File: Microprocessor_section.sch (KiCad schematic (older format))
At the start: 14 parts, among them J15 Conn_01x06_Male, SW1 K2-1102SP-C4SC-04, U5 ESP32-WROOM-32D

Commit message: Export fabrication files
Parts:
- J15: LCSC (none) -> C124380
- JP3, JP4: LCSC (none) -> C160332
- U5: LCSC (none) -> C473012
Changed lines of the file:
@@
 F 2 "Connector_PinHeader_2.54mm:PinHeader_1x06_P2.54mm_Vertical" H 2000 2200 50  0001 C CNN
 F 3 "~" H 2000 2200 50  0001 C CNN
+F 4 "C124380" H 2000 2200 50  0001 C CNN "LCSC"
 	1    2000 2200
 	1    0    0    -1
@@
 F 2 "RF_Module:ESP32-WROOM-32" H 6500 2500 50  0001 C CNN
 F 3 "https://www.espressif.com/sites/default/files/documentation/esp32-wroom-32d_esp32-wroom-32u_datasheet_en.pdf" H 6200 4050 50  0001 C CNN
+F 4 "C473012" H 6500 4000 50  0001 C CNN "LCSC"
 	1    6500 4000
 	1    0    0    -1
@@
 F 2 "Connector_PinHeader_2.54mm:PinHeader_1x02_P2.54mm_Vertical" H 2000 4100 50  0001 C CNN
 F 3 "~" H 2000 4100 50  0001 C CNN
+F 4 "C160332" H 2000 4100 50  0001 C CNN "LCSC"
 	1    2000 4100
 	1    0    0    1
@@
 F 2 "Connector_PinHeader_2.54mm:PinHeader_1x02_P2.54mm_Vertical" H 3800 4000 50  0001 C CNN
 F 3 "~" H 3800 4000 50  0001 C CNN
+F 4 "C160332" H 3800 4000 50  0001 C CNN "LCSC"
 	1    3800 4000
 	1    0    0    -1

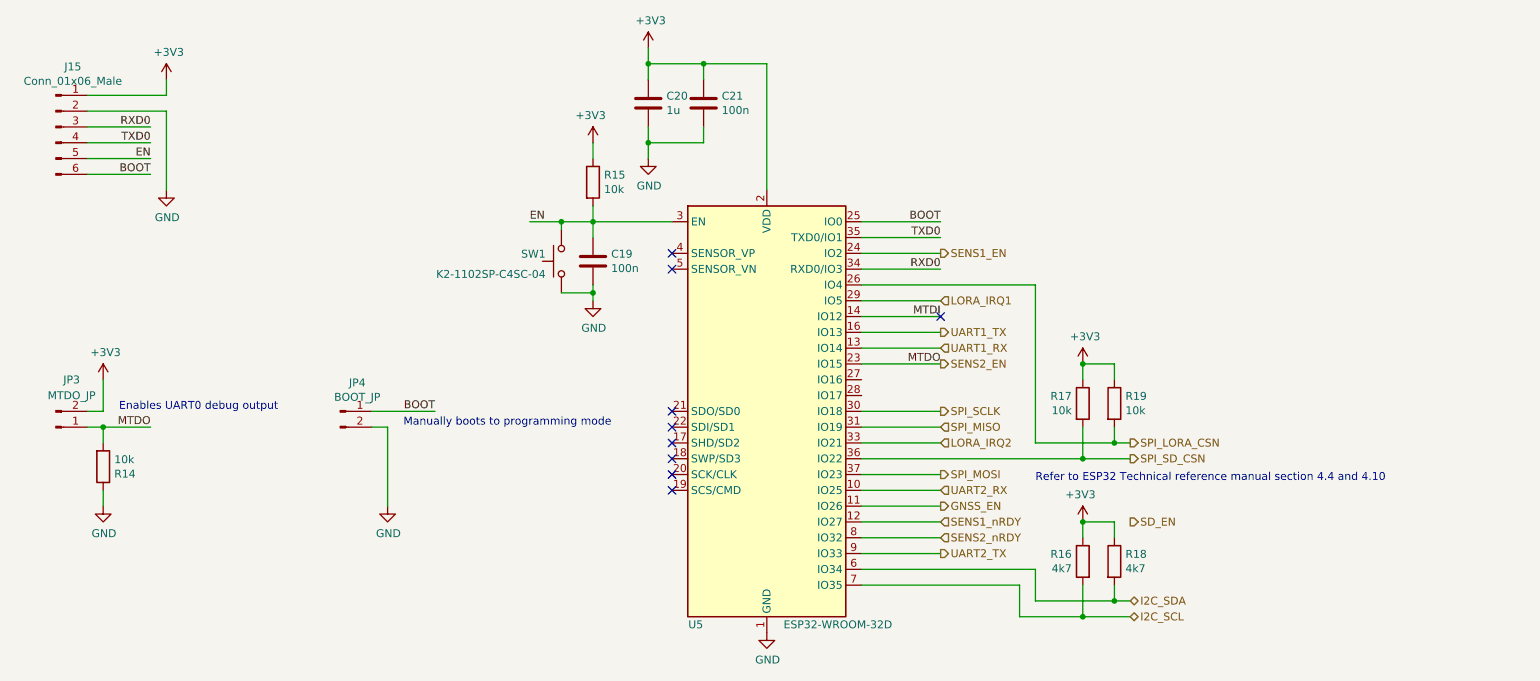
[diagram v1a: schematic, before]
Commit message: Start changing design for long term chambers
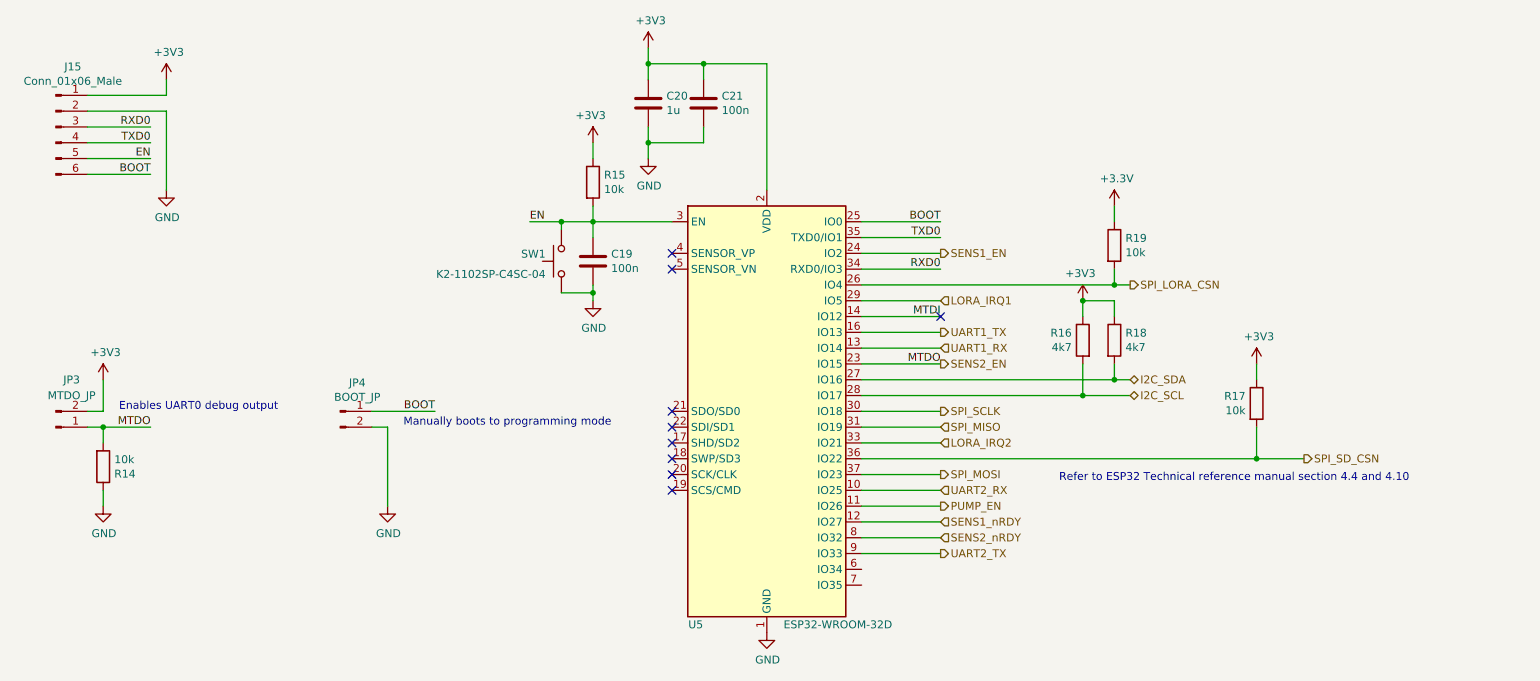
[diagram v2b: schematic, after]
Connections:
- net I2C_SCL: now also U5.28 (IO17); no longer U5.7 (IO35)
- net I2C_SDA: now also U5.27 (IO16); no longer U5.6 (IO34)
- net GNSS_EN renamed PUMP_EN
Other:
- moved on the sheet: R16, R17, R18, R19
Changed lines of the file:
@@
 $Descr A4 11693 8268
 encoding utf-8
-Sheet 9 9
+Sheet 8 9
 Title ""
 Date ""
@@
 $EndComp
 Wire Wire Line
-	8500 5100 8500 5300
-Wire Wire Line
-	8500 5300 8800 5300
-Connection ~ 8500 4700
-Wire Wire Line
-	8700 4200 8800 4200
-Connection ~ 8700 4200
-Wire Wire Line
-	8700 4100 8700 4200
-Wire Wire Line
-	8500 4300 8800 4300
-Connection ~ 8500 4300
-Wire Wire Line
-	8500 4100 8500 4300
-Wire Wire Line
-	8700 5200 8800 5200
-Wire Wire Line
-	8500 4700 8700 4700
-Wire Wire Line
-	8500 3700 8700 3700
-Wire Wire Line
-	8700 3700 8700 3800
+	8700 3200 8800 3200
+Connection ~ 8700 3200
+Wire Wire Line
+	8700 3100 8700 3200
 $Comp
 L power:GND #PWR064
@@
 	7100 4800 7600 4800
 Wire Wire Line
-	7100 4600 7600 4600
-Wire Wire Line
 	7100 4700 7600 4700
 Wire Wire Line
@@
 Text HLabel 7600 4000 2    50   Output ~ 0
 SPI_SCLK
-Text HLabel 8800 4700 2    50   Output ~ 0
-SD_EN
 Text HLabel 7600 4200 2    50   Input ~ 0
 LORA_IRQ2
 Text HLabel 7600 3300 2    50   Input ~ 0
 LORA_IRQ1
-Text HLabel 7600 4600 2    50   Output ~ 0
-GNSS_EN
 Text HLabel 7600 4800 2    50   Input ~ 0
 SENS2_nRDY
@@
 	6100 1800 5750 1800
 Connection ~ 6100 1800
-Connection ~ 8500 3700
-Wire Wire Line
-	8500 3800 8500 3700
-$Comp
-L power:+3V3 #PWR066
-U 1 1 60A5A46E
-P 8500 3700
-F 0 "#PWR066" H 8500 3550 50  0001 C CNN
-F 1 "+3V3" H 8515 3873 50  0000 C CNN
-F 2 "" H 8500 3700 50  0001 C CNN
-F 3 "" H 8500 3700 50  0001 C CNN
-	1    8500 3700
-	1    0    0    -1
-$EndComp
 $Comp
 L Device:R R19
 U 1 1 60A5A468
-P 8700 3950
-F 0 "R19" H 8770 3996 50  0000 L CNN
-F 1 "10k" H 8770 3905 50  0000 L CNN
-F 2 "Resistor_SMD:R_0603_1608Metric" V 8630 3950 50  0001 C CNN
-F 3 "~" H 8700 3950 50  0001 C CNN
-F 4 "C25804" H 8700 3950 50  0001 C CNN "LCSC"
-	1    8700 3950
-	1    0    0    -1
-$EndComp
-$Comp
-L Device:R R17
-U 1 1 60A5A462
-P 8500 3950
-F 0 "R17" H 8430 3996 50  0000 R CNN
-F 1 "10k" H 8430 3905 50  0000 R CNN
-F 2 "Resistor_SMD:R_0603_1608Metric" V 8430 3950 50  0001 C CNN
-F 3 "~" H 8500 3950 50  0001 C CNN
-F 4 "C25804" H 8500 3950 50  0001 C CNN "LCSC"
-	1    8500 3950
-	1    0    0    -1
-$EndComp
-Wire Wire Line
-	8500 4800 8500 4700
-Wire Wire Line
-	8700 4800 8700 4700
-Wire Wire Line
-	8700 5200 8700 5100
-$Comp
-L power:+3V3 #PWR065
-U 1 1 60A5400B
-P 8500 4700
-F 0 "#PWR065" H 8500 4550 50  0001 C CNN
-F 1 "+3V3" H 8515 4873 50  0000 C CNN
-F 2 "" H 8500 4700 50  0001 C CNN
-F 3 "" H 8500 4700 50  0001 C CNN
-	1    8500 4700
-	-1   0    0    -1
-$EndComp
-$Comp
-L Device:R R16
-U 1 1 60A50D69
-P 8500 4950
-F 0 "R16" H 8570 4996 50  0000 L CNN
-F 1 "4k7" H 8570 4905 50  0000 L CNN
-F 2 "Resistor_SMD:R_0603_1608Metric" V 8430 4950 50  0001 C CNN
-F 3 "~" H 8500 4950 50  0001 C CNN
-F 4 "C23162" H 8500 4950 50  0001 C CNN "LCSC"
-	1    8500 4950
-	-1   0    0    -1
-$EndComp
-$Comp
-L Device:R R18
-U 1 1 60A501AF
-P 8700 4950
-F 0 "R18" H 8770 4996 50  0000 L CNN
-F 1 "4k7" H 8770 4905 50  0000 L CNN
-F 2 "Resistor_SMD:R_0603_1608Metric" V 8630 4950 50  0001 C CNN
-F 3 "~" H 8700 4950 50  0001 C CNN
-F 4 "C23162" H 8700 4950 50  0001 C CNN "LCSC"
-	1    8700 4950
+P 8700 2950
+F 0 "R19" H 8770 2996 50  0000 L CNN
+F 1 "10k" H 8770 2905 50  0000 L CNN
+F 2 "Resistor_SMD:R_0603_1608Metric" V 8630 2950 50  0001 C CNN
+F 3 "~" H 8700 2950 50  0001 C CNN
+F 4 "C25804" H 8700 2950 50  0001 C CNN "LCSC"
+	1    8700 2950
 	1    0    0    -1
 $EndComp
@@
 Wire Wire Line
 	7600 3600 7100 3600
-Text HLabel 8800 4300 2    50   Output ~ 0
-SPI_SD_CSN
-Text HLabel 8800 4200 2    50   Output ~ 0
+Text HLabel 8800 3200 2    50   Output ~ 0
 SPI_LORA_CSN
-Text HLabel 8800 5200 2    50   BiDi ~ 0
-I2C_SDA
-Text HLabel 8800 5300 2    50   BiDi ~ 0
-I2C_SCL
 Text HLabel 7600 3600 2    50   Input ~ 0
 UART1_RX
@@
 Text HLabel 7600 4900 2    50   Output ~ 0
 UART2_TX
-Text Notes 8200 4450 0    50   ~ 0
-Refer to ESP32 Technical reference manual section 4.4 and 4.10\n
 NoConn ~ 7600 3400
 Wire Wire Line
@@
 	0    -1   -1   0
 $EndComp
-Connection ~ 8700 5200
-Connection ~ 8500 5300
-Wire Wire Line
-	7100 4300 8500 4300
-Wire Wire Line
-	7100 3200 8200 3200
-Wire Wire Line
-	8200 3200 8200 4200
-Wire Wire Line
-	8200 4200 8700 4200
-Wire Wire Line
-	8200 5200 8700 5200
-Wire Wire Line
-	8100 5300 8500 5300
-Wire Wire Line
-	7100 5000 8200 5000
-Wire Wire Line
-	8200 5000 8200 5200
-Wire Wire Line
-	8100 5300 8100 5100
-Wire Wire Line
-	8100 5100 7100 5100
+Wire Wire Line
+	7100 3200 8700 3200
+Text Notes 8350 4450 0    50   ~ 0
+Refer to ESP32 Technical reference manual section 4.4 and 4.10\n
+Text HLabel 9900 4300 2    50   Output ~ 0
+SPI_SD_CSN
+$Comp
+L Device:R R17
+U 1 1 60A5A462
+P 9600 3950
+F 0 "R17" H 9530 3996 50  0000 R CNN
+F 1 "10k" H 9530 3905 50  0000 R CNN
+F 2 "Resistor_SMD:R_0603_1608Metric" V 9530 3950 50  0001 C CNN
+F 3 "~" H 9600 3950 50  0001 C CNN
+F 4 "C25804" H 9600 3950 50  0001 C CNN "LCSC"
+	1    9600 3950
+	1    0    0    -1
+$EndComp
+$Comp
+L power:+3V3 #PWR066
+U 1 1 60A5A46E
+P 9600 3700
+F 0 "#PWR066" H 9600 3550 50  0001 C CNN
+F 1 "+3V3" H 9615 3873 50  0000 C CNN
+F 2 "" H 9600 3700 50  0001 C CNN
+F 3 "" H 9600 3700 50  0001 C CNN
+	1    9600 3700
+	1    0    0    -1
+$EndComp
+Wire Wire Line
+	9600 3800 9600 3700
+Wire Wire Line
+	9600 4100 9600 4300
+Connection ~ 9600 4300
+Wire Wire Line
+	9600 4300 9900 4300
+Connection ~ 8500 3900
+Connection ~ 8700 3800
+Text HLabel 8800 3900 2    50   BiDi ~ 0
+I2C_SCL
+Text HLabel 8800 3800 2    50   BiDi ~ 0
+I2C_SDA
+$Comp
+L Device:R R18
+U 1 1 60A501AF
+P 8700 3550
+F 0 "R18" H 8770 3596 50  0000 L CNN
+F 1 "4k7" H 8770 3505 50  0000 L CNN
+F 2 "Resistor_SMD:R_0603_1608Metric" V 8630 3550 50  0001 C CNN
+F 3 "~" H 8700 3550 50  0001 C CNN
+F 4 "C23162" H 8700 3550 50  0001 C CNN "LCSC"
+	1    8700 3550
+	1    0    0    -1
+$EndComp
+$Comp
+L Device:R R16
+U 1 1 60A50D69
+P 8500 3550
+F 0 "R16" H 8570 3596 50  0000 L CNN
+F 1 "4k7" H 8570 3505 50  0000 L CNN
+F 2 "Resistor_SMD:R_0603_1608Metric" V 8430 3550 50  0001 C CNN
+F 3 "~" H 8500 3550 50  0001 C CNN
+F 4 "C23162" H 8500 3550 50  0001 C CNN "LCSC"
+	1    8500 3550
+	-1   0    0    -1
+$EndComp
+$Comp
+L power:+3V3 #PWR065
+U 1 1 60A5400B
+P 8500 3300
+F 0 "#PWR065" H 8500 3150 50  0001 C CNN
+F 1 "+3V3" H 8515 3473 50  0000 C CNN
+F 2 "" H 8500 3300 50  0001 C CNN
+F 3 "" H 8500 3300 50  0001 C CNN
+	1    8500 3300
+	-1   0    0    -1
+$EndComp
+Wire Wire Line
+	8700 3800 8700 3700
+Wire Wire Line
+	8700 3400 8700 3300
+Wire Wire Line
+	8500 3400 8500 3300
+Wire Wire Line
+	8500 3300 8700 3300
+Wire Wire Line
+	8700 3800 8800 3800
+Connection ~ 8500 3300
+Wire Wire Line
+	8500 3900 8800 3900
+Wire Wire Line
+	8500 3700 8500 3900
+Wire Wire Line
+	7100 3900 8500 3900
+Wire Wire Line
+	7100 3800 8700 3800
+Wire Wire Line
+	7100 4300 9600 4300
+Text HLabel 7600 4600 2    50   Output ~ 0
+PUMP_EN
+Wire Wire Line
+	7100 4600 7600 4600
+$Comp
+L power:+3.3V #PWR?
+U 1 1 60C14EF9
+P 8700 2700
+F 0 "#PWR?" H 8700 2550 50  0001 C CNN
+F 1 "+3.3V" H 8715 2873 50  0000 C CNN
+F 2 "" H 8700 2700 50  0001 C CNN
+F 3 "" H 8700 2700 50  0001 C CNN
+	1    8700 2700
+	1    0    0    -1
+$EndComp
+Wire Wire Line
+	8700 2800 8700 2700
 $EndSCHEMATC

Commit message: Finalize schematic
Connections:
- net LORA_IRQ2: now also U5.6 (IO34); no longer U5.33 (IO21)
- new net TEMPSENSOR: U5.33 (IO21)
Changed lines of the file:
@@
 $EndComp
 Wire Wire Line
-	7100 4200 7600 4200
+	7100 5000 7600 5000
 Wire Wire Line
 	7100 3300 7600 3300
@@
 Text HLabel 7600 4000 2    50   Output ~ 0
 SPI_SCLK
-Text HLabel 7600 4200 2    50   Input ~ 0
+Text HLabel 7600 5000 2    50   Input ~ 0
 LORA_IRQ2
 Text HLabel 7600 3300 2    50   Input ~ 0
@@
 Wire Wire Line
 	8700 2800 8700 2700
+Text HLabel 7600 4200 2    50   Input ~ 0
+TEMPSENSOR
+Wire Wire Line
+	7100 4200 7600 4200
 $EndSCHEMATC

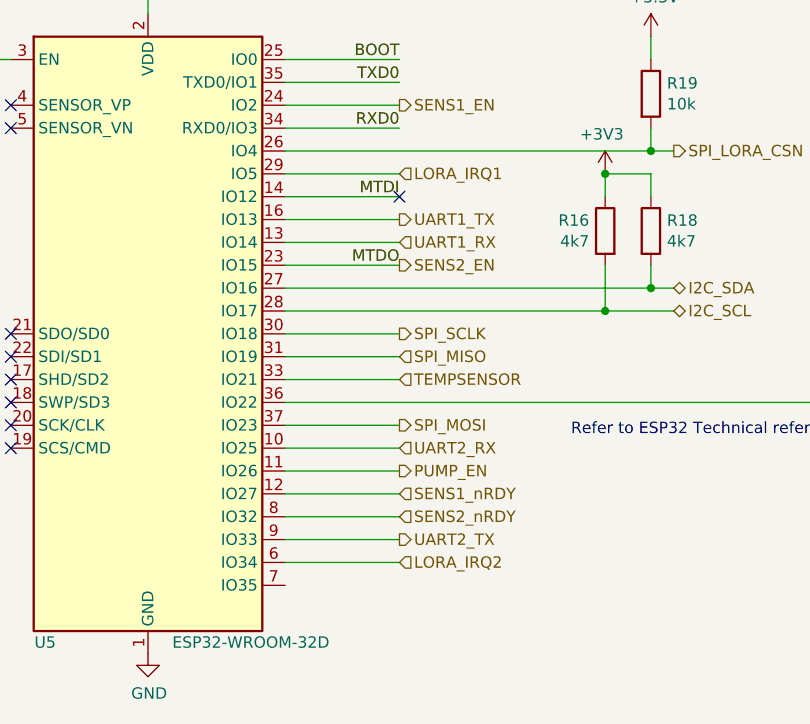
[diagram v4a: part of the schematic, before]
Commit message: Finish routing of Rev 1
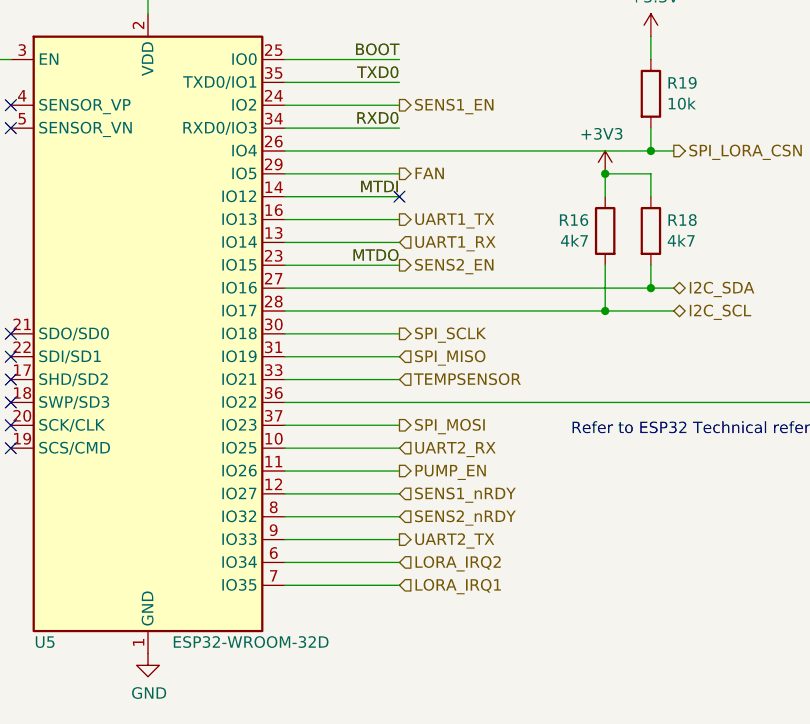
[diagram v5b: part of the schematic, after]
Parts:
- SW1: LCSC https://lcsc.com/product-detail/Tactile-Switches_Korean-Hro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 -> C127509
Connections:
- net LORA_IRQ1: now also U5.7 (IO35); no longer U5.29 (IO5)
- new net FAN: U5.29 (IO5)
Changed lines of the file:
@@
 $Descr A4 11693 8268
 encoding utf-8
-Sheet 8 9
+Sheet 8 10
 Title ""
 Date ""
@@
 	7100 5000 7600 5000
 Wire Wire Line
-	7100 3300 7600 3300
+	7100 5100 7600 5100
 Wire Wire Line
 	7100 4100 7600 4100
@@
 Text HLabel 7600 5000 2    50   Input ~ 0
 LORA_IRQ2
-Text HLabel 7600 3300 2    50   Input ~ 0
+Text HLabel 7600 5100 2    50   Input ~ 0
 LORA_IRQ1
 Text HLabel 7600 4800 2    50   Input ~ 0
@@
 F 2 "co2_sensor_node:K2-1102SP-xxxC" H 5200 3250 50  0001 C CNN
 F 3 "https://datasheet.lcsc.com/szlcsc/1811082113_Korean-Hroparts-Elec-K2-1102SP-C4SC-04_C127509.pdf" H 5200 3250 50  0001 C CNN
-F 4 "https://lcsc.com/product-detail/Tactile-Switches_Korean-Hroparts-Elec-K2-1102SP-C4SC-04_C127509.html/?href=jlc-SMT" V 5200 3050 50  0001 C CNN "LCSC"
+F 4 "C127509" V 5200 3050 50  0001 C CNN "LCSC"
 	1    5200 3050
 	0    -1   -1   0
@@
 Wire Wire Line
 	7100 4200 7600 4200
+Text HLabel 7600 3300 2    50   Output ~ 0
+FAN
+Wire Wire Line
+	7100 3300 7600 3300
 $EndSCHEMATC
